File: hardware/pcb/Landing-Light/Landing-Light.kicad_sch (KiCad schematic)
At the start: 56 parts, among them J1 Conn_01x04, J2 2012670005, Q2 NMOS, Q3 NMOS, Q4 PMOS, SW2 SW_SP3T, SW3 SW_SPDT, U1 BQ25172DSGR, U3 TPS61200DRC

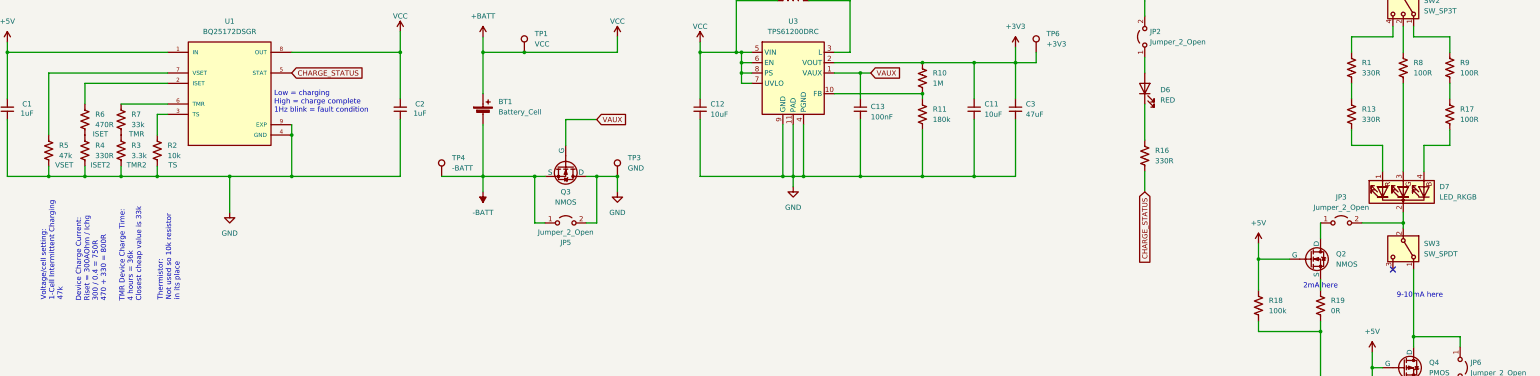
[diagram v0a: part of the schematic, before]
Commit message: Tidy resistor values
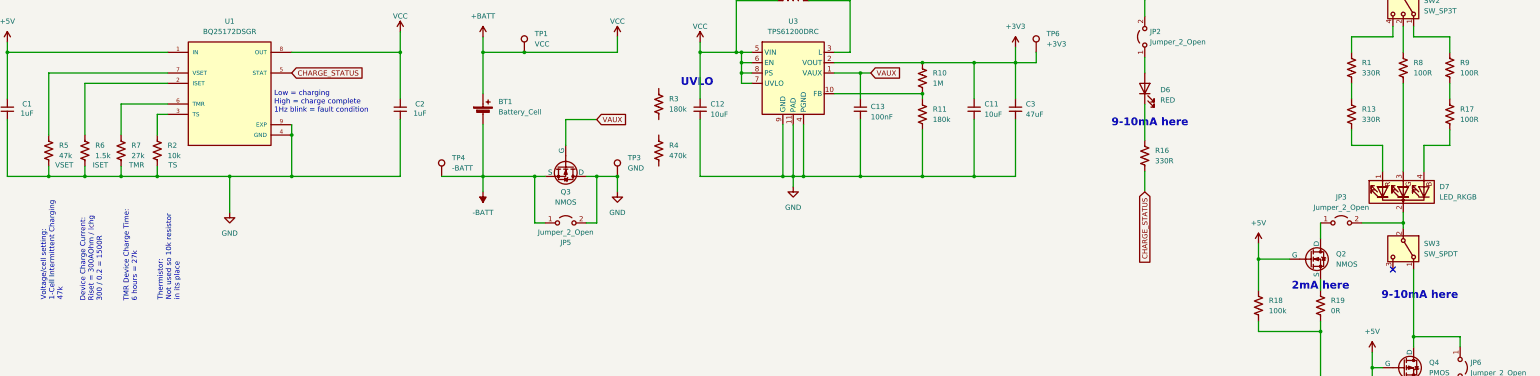
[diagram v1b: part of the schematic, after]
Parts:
- R3: value 3.3k -> 180k; footprint Resistor_SMD:R_0402_1005Metric -> Resistor_SMD:R_0603_1608Metric; LCSC C25890 -> C22827
- R4: value 330R -> 470k; LCSC C25104 -> C25790
- R6: value 470R -> 1.5k; LCSC C25117 -> C25867
- R7: value 33k -> 27k; LCSC C25779 -> C25771
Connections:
- net GND: now also R6.2, R7.2; no longer R3.2, R4.2
- net at R4.1: no longer R6.2
- net at R3.1: no longer R7.2
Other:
- note added: "Device Charge Current: Riset = 300AOhm / Ichg 300 / 0.2 = 1500R"
- note added: "TMR Device Charge Time: 6 hours = 27k"
- note added: "UVLO"
- note removed: "Device Charge Current: Riset = 300AOhm / Ichg 300 / 0.4 = 750R 470 + 330 = 800R"
- note removed: "TMR Device Charge Time: 4 hours = 36k Closest cheap value is 33k"
- moved on the sheet: R6, R7

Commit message: Final layout checks
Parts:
- removed R17: 100R, Resistor_SMD:R_0402_1005Metric, symbol Device:R_US
- added JP4: Jumper_2_Open, Jumper:SolderJumper-2_P1.3mm_Open_RoundedPad1.0x1.5mm, symbol Jumper:Jumper_2_Open
- Q2, Q3: footprint Package_TO_SOT_SMD:SOT-23-3 -> Landing-Light:SOT-23-3-JLCPCB
- R1, R13: value 330R -> 75R; LCSC C25104 -> C25133
- R19: value 0R -> 220R; LCSC C17168 -> C25091
- R8, R9: value 100R -> 75R; LCSC C25076 -> C25133
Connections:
- net +BATT: now also R3.1, JP4.1 (A); no longer U3.7 (UVLO)
- net GND: now also R4.2
- net at R9.2: now also D7.4 (BA)
- net at R4.1: now also R3.2, U3.7 (UVLO), JP4.2 (B)
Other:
- note added: "Device Charge Current: Riset = 300AOhm / Ichg 300 / 0.2 = 1.5k"
- note added: "Switches Mosfet Pinout"
- note added: "Vf = 2.6, Vs = 5v, I = 5mA R ="
- note added: "Vs = 3V3, I = 8mA Red: Vf = 2.2 -> R = 150 Green: Vf = 2.7 -> R = 75 Blue: Vf = 2.7 -> R = 75"
- note removed: "Device Charge Current: Riset = 300AOhm / Ichg 300 / 0.2 = 1500R"
- note removed: "UVLO"
- moved on the sheet: C11, C12, C13, C3, D6, JP2, L2, R10, R11, R16, R3, R4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

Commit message: v1 Production
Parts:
- U3: LCSC (none) -> C140320
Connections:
- net -BATT: now also Q3.1 (D); no longer Q3.3 (S)
- net GND: now also Q3.3 (S); no longer Q3.1 (D)
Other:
- note removed: "Switches Mosfet Pinout"
- moved on the sheet: BT1, JP5, Q3, TP1, TP3, TP4

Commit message: Final footprint fixes
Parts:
- SW2, SW3: now in the parts list
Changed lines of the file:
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@@
 		(unit 1)
 		(exclude_from_sim no)
-		(in_bom no)
+		(in_bom yes)
 		(on_board yes)
 		(dnp no)
@@
 		(unit 1)
 		(exclude_from_sim no)
-		(in_bom no)
-		(on_board yes)
-		(dnp no)
+		(in_bom yes)
+		(on_board yes)
+		(dnp no)

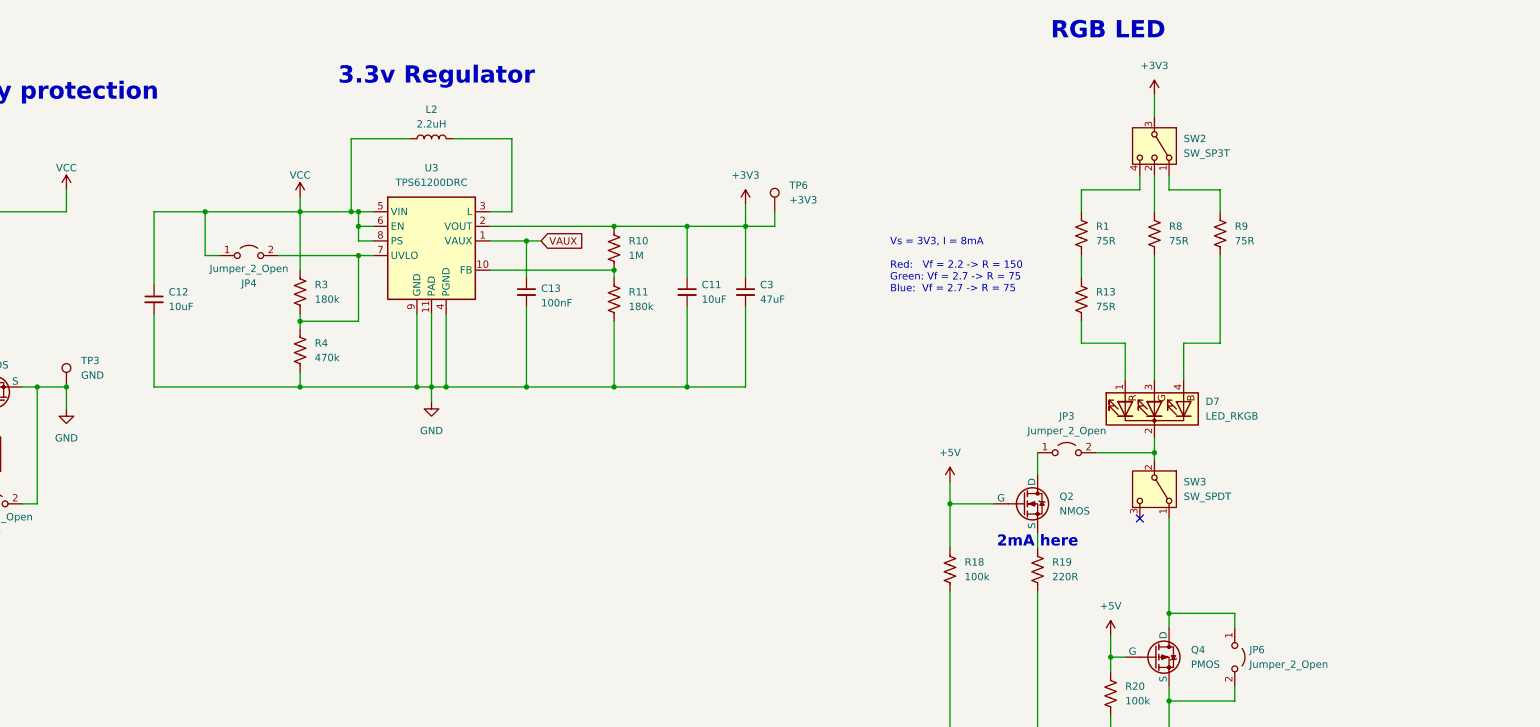
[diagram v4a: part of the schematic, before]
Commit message: Comments added after first production run
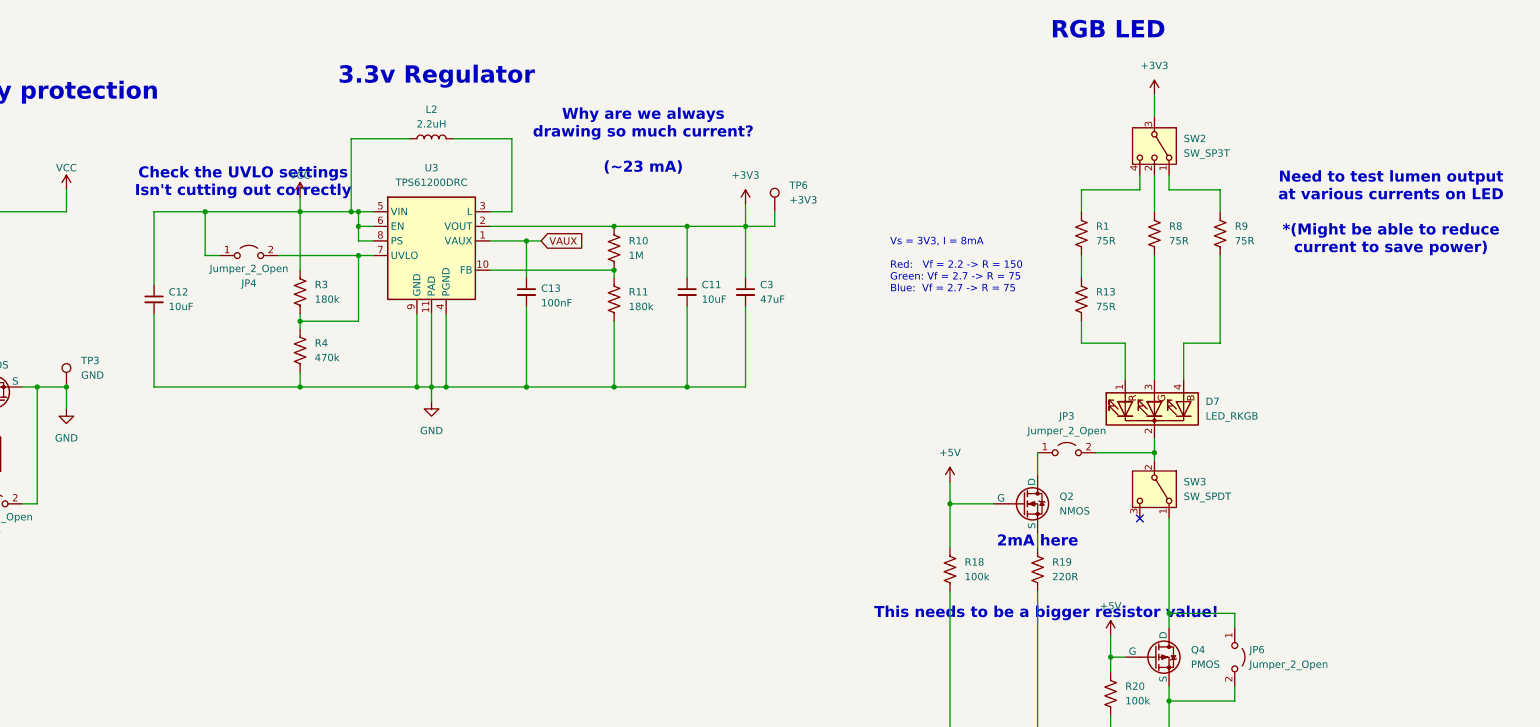
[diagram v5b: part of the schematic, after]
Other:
- note added: "Check the UVLO settings Isn't cutting out correctly"
- note added: "Need to test lumen output at various currents on LED *(Might be able to reduce current to save power)"
- note added: "This needs to be a bigger resistor value!"
- note added: "Why are we always drawing so much current? (~23 mA)"
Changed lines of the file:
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@@
+		)
+	)
+	(text "This needs to be a bigger resistor value!"
+		(exclude_from_sim no)
+		(at 358.394 123.19 0)
+		(effects
+			(font
+				(size 1.905 1.905)
+				(thickness 0.381)
+				(bold yes)
+				(color 255 0 0 1)
+			)
 		)
 	)
@@
 		)
 	)
+	(text "Need to test lumen output \nat various currents on LED\n\n*(Might be able to reduce\ncurrent to save power)"
+		(exclude_from_sim no)
+		(at 418.338 53.594 0)
+		(effects
+			(font
+				(size 1.905 1.905)
+				(thickness 0.381)
+				(bold yes)
+				(color 255 0 0 1)
+			)
+		)
+	)
 	(text "RGB LED"
 		(exclude_from_sim no)
@@
 		)
 	)
+	(text "Why are we always \ndrawing so much current?\n\n(~23 mA)"
+		(exclude_from_sim no)
+		(at 288.29 41.148 0)
+		(effects
+			(font
+				(size 1.905 1.905)
+				(thickness 0.381)
+				(bold yes)
+				(color 255 0 0 1)
+			)
+		)
+	)
+	(text "Check the UVLO settings\nIsn't cutting out correctly"
+		(exclude_from_sim no)
+		(at 218.694 48.26 0)
+		(effects
+			(font
+				(size 1.905 1.905)
+				(thickness 0.381)
+				(bold yes)
+				(color 255 0 0 1)
+			)
+		)
+	)

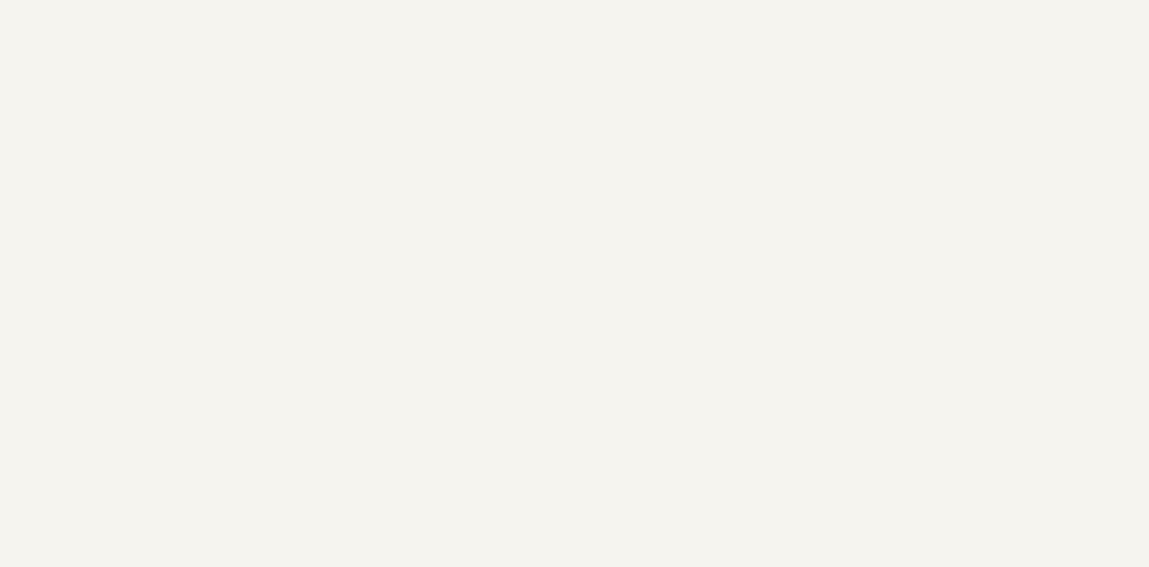
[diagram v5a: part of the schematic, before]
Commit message: Adding new pogo connector
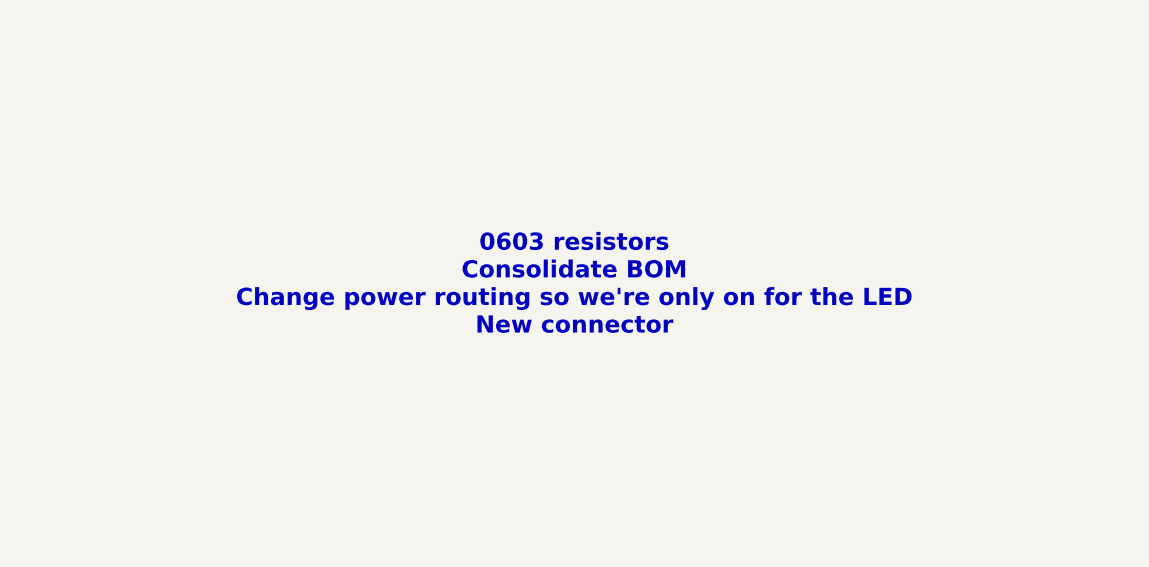
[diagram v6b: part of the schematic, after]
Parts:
- J1: footprint Landing-Light:70AAJ-4-F1G -> MHCI:399-10-104-10-008000
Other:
- note added: "0603 resistors Consolidate BOM Change power routing so we're only on for the LED New connector"
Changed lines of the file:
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@@
 		)
 	)
+	(text "0603 resistors\nConsolidate BOM\nChange power routing so we're only on for the LED\nNew connector"
+		(exclude_from_sim no)
+		(at 188.468 146.05 0)
+		(effects
+			(font
+				(size 1.905 1.905)
+				(thickness 0.381)
+				(bold yes)
+				(color 255 0 0 1)
+			)
+		)
+	)
 	(text "Vf = 2.6, Vs = 5v, I = 5mA\nR = \n"
 		(exclude_from_sim no)
@@
 			)
 		)
-		(property "Footprint" "Landing-Light:70AAJ-4-F1G"
+		(property "Footprint" "MHCI:399-10-104-10-008000"
 			(at 53.34 179.07 0)
 			(effects

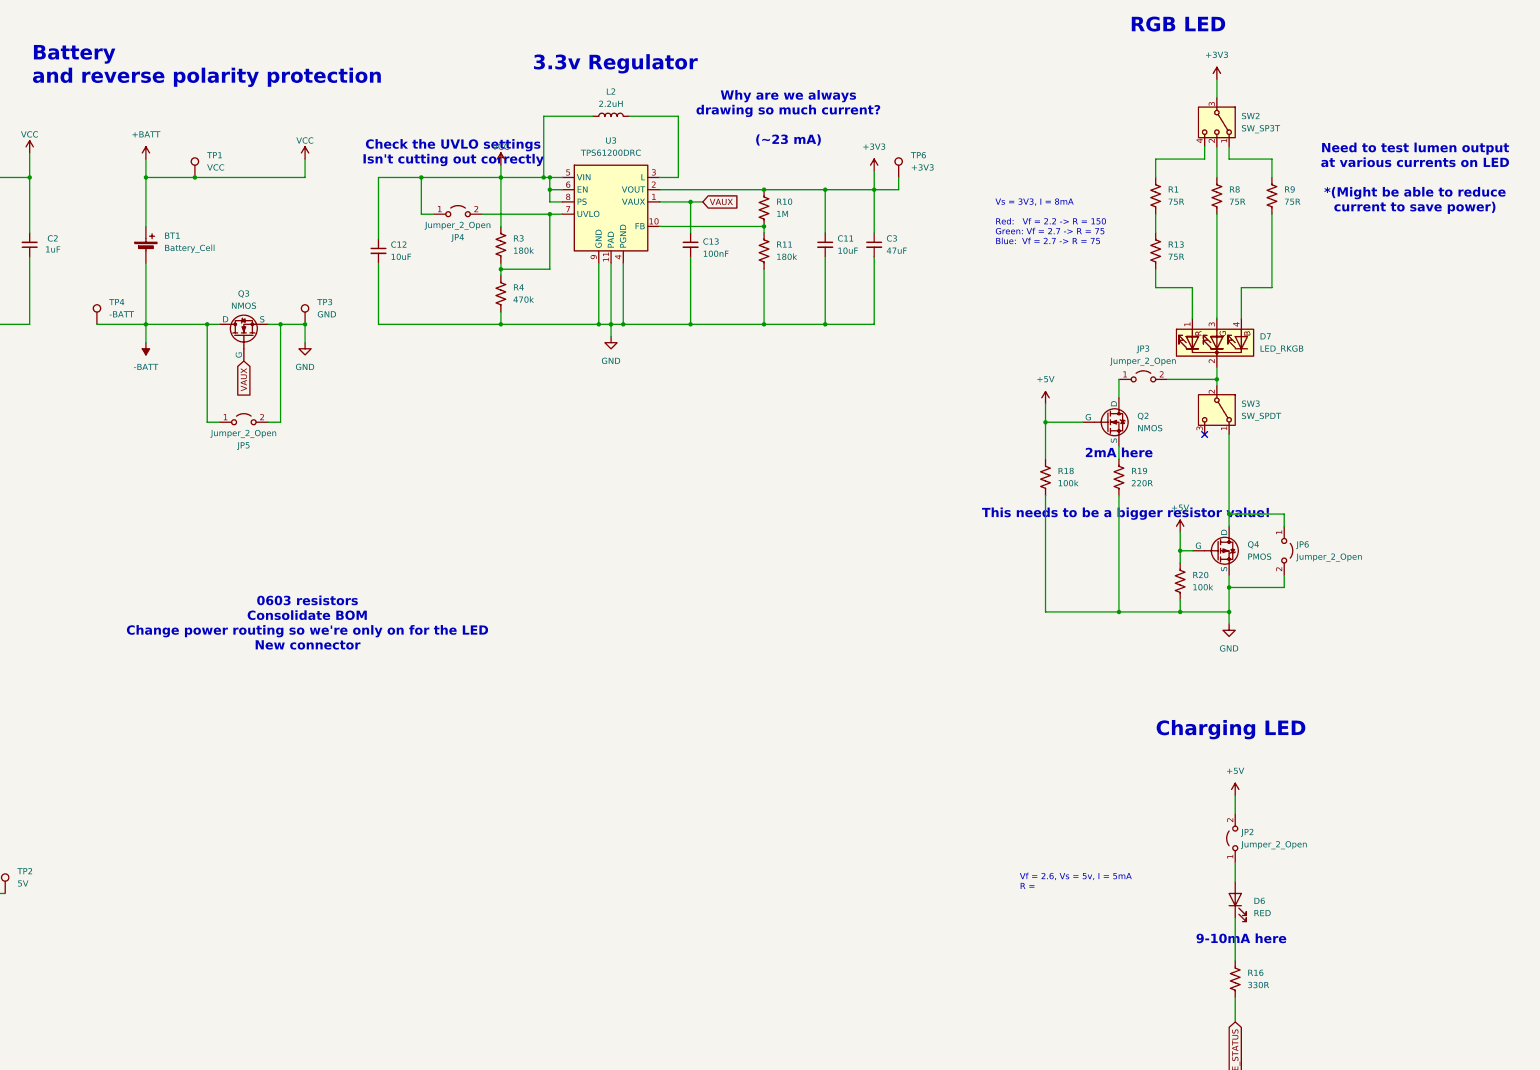
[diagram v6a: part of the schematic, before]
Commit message: Update power routing
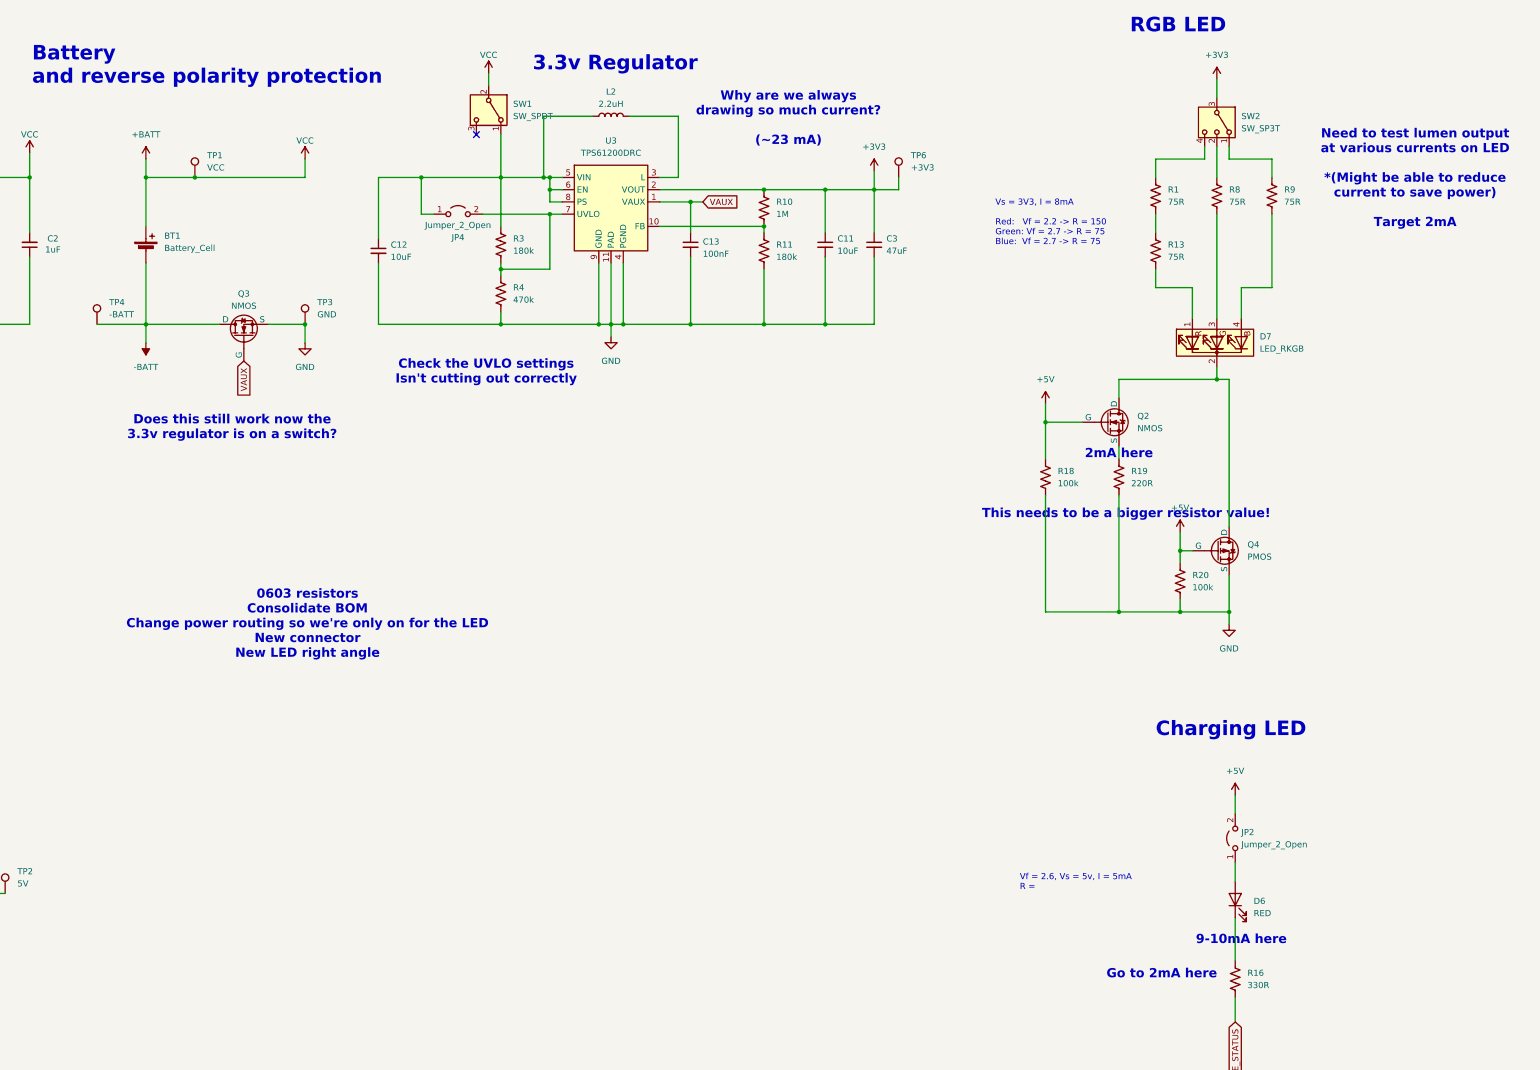
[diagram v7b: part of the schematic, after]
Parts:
- removed JP3, JP5, JP6: Jumper_2_Open, Jumper:SolderJumper-2_P1.3mm_Open_RoundedPad1.0x1.5mm, symbol Jumper:Jumper_2_Open
- removed SW3: SW_SPDT, Landing-Light:SSSS810201, symbol Switch:SW_SPDT
- added SW1: SW_SPDT, Landing-Light:SSSS810201, symbol Switch:SW_SPDT
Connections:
- net +BATT: now also SW1.2 (B); no longer C12.1, JP4.1 (A), L2.1, R3.1, U3.5 (VIN), U3.6 (EN), U3.8 (PS)
- net at Q4.3 (D): now also D7.2 (K), Q2.1 (D)
- new net: C12.1, JP4.1 (A), L2.1, R3.1, SW1.1 (A), U3.5 (VIN), U3.6 (EN), U3.8 (PS)
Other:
- note added: "0603 resistors Consolidate BOM Change power routing so we're only on for the LED New connector New LED right angle"
- note added: "Does this still work now the 3.3v regulator is on a switch?"
- note added: "Go to 2mA here"
- note added: "Need to test lumen output at various currents on LED *(Might be able to reduce current to save power) Target 2mA"
- note removed: "0603 resistors Consolidate BOM Change power routing so we're only on for the LED New connector"
- note removed: "Need to test lumen output at various currents on LED *(Might be able to reduce current to save power)"
